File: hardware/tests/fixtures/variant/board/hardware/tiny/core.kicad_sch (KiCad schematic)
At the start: 2 parts

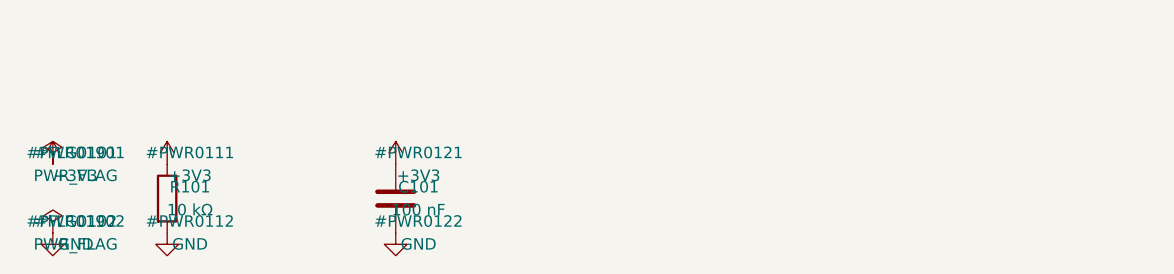
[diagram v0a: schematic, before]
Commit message: odapkit variant: absent-state check and software outputs per variant (RFC 0011 rules 2, 7, 8)
The absent-state check reads the XML netlist with the variant's resolution: every
net a dnp block touches is classified with the fitted parts only (single-pin,
floating, rail without source, defined) and matched to a declared absent state
from the block sheets' interface tables or the record's absent_state list; nets
touched only by other unfitted parts are reported when they become single-pin.
Findings absent.floating, absent.single-pin, absent.rail-unsourced,
absent.undeclared, absent.declared-mismatch and absent.not-applicable.

apply writes absent-state.json (opendap.variant-absent-state/v1),
software/capabilities.json (opendap.variant-capabilities/v1, a fragment for the
device description; consumer side open) and software/devicetree.json
(opendap.variant-devicetree/v1) with variant.dtso, status okay or disabled per
block node, blocks with no node listed as skipped. check runs the absent-state
check per variant. Block records gain structured absent_state and software;
the Markdown catalog reads its Absent state and Software rows. The fixture's
sensor sheet carries an interface table.

Co-Authored-By: Claude Opus 5.5 <noreply@anthropic.com>
Claude-Session: https://claude.ai/code/session_01Ei262h3TpgY9vyfNLMi5Mn
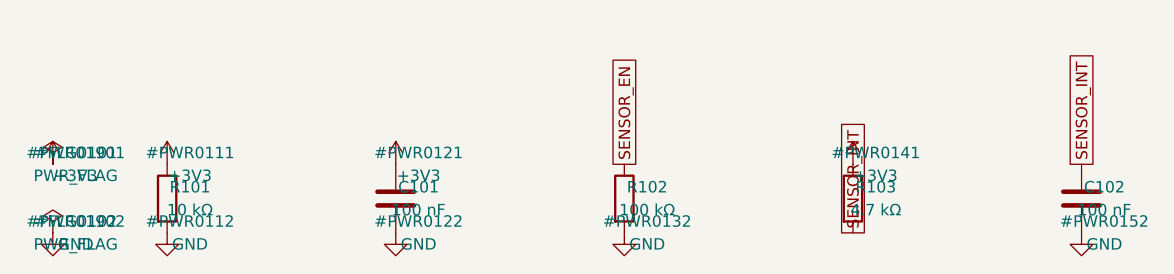
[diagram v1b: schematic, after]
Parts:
- added C102: 100 nF, Capacitor_SMD:C_0402_1005Metric, symbol Device:C
- added R102: 100 kΩ, Resistor_SMD:R_0603_1608Metric, symbol Device:R
- added R103: 4.7 kΩ, Resistor_SMD:R_0603_1608Metric, symbol Device:R
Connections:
- net +3V3: now also R103.1
- net GND: now also C102.2, R102.2
- new net SENSOR_EN: R102.1
- new net SENSOR_INT: C102.1, R103.2
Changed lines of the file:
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@@
   (instances (project "tiny" (path "/66a81b00-37dd-53f5-81ba-daabee42749a/791f5bf8-41bc-56d1-9e1d-b6f01e930073" (reference "#PWR0122") (unit 1))))
+)
+(symbol (lib_id "Device:R") (at 114.3 60.96 0) (unit 1) (body_style 1) (exclude_from_sim no) (in_bom yes) (on_board yes) (dnp no)
+  (property "Reference" "R102" (at 116.84 59.69 0) (effects (font (size 1.27 1.27))))
+  (property "Value" "100 kΩ" (at 116.84 62.230000000000004 0) (effects (font (size 1.27 1.27))))
+  (property "Footprint" "Resistor_SMD:R_0603_1608Metric" (at 114.3 60.96 0) (effects (font (size 1.27 1.27)) (hide yes)))
+  (property "Datasheet" "" (at 114.3 60.96 0) (effects (font (size 1.27 1.27)) (hide yes)))
+  (property "Block" "blk.core" (at 114.3 60.96 0) (effects (font (size 1.27 1.27)) (hide yes)))
+  (property "MPN" "RC0603FR-07100KL" (at 114.3 60.96 0) (effects (font (size 1.27 1.27)) (hide yes)))
+  (property "Manufacturer" "YAGEO" (at 114.3 60.96 0) (effects (font (size 1.27 1.27)) (hide yes)))
+  (pin "1")
+  (pin "2")
+  (instances (project "tiny" (path "/66a81b00-37dd-53f5-81ba-daabee42749a/791f5bf8-41bc-56d1-9e1d-b6f01e930073" (reference "R102") (unit 1))))
+)
+(global_label "SENSOR_EN" (shape passive) (at 114.3 57.15 90) (effects (font (size 1.27 1.27)) (justify left)))
+(symbol (lib_id "power:GND") (at 114.3 64.77 0) (unit 1) (body_style 1) (exclude_from_sim no) (in_bom no) (on_board no) (dnp no)
+  (property "Reference" "#PWR0132" (at 116.84 63.49999999999999 0) (effects (font (size 1.27 1.27))))
+  (property "Value" "GND" (at 116.84 66.03999999999999 0) (effects (font (size 1.27 1.27))))
+  (property "Footprint" "" (at 114.3 64.77 0) (effects (font (size 1.27 1.27)) (hide yes)))
+  (property "Datasheet" "" (at 114.3 64.77 0) (effects (font (size 1.27 1.27)) (hide yes)))
+  (pin "1")
+  (instances (project "tiny" (path "/66a81b00-37dd-53f5-81ba-daabee42749a/791f5bf8-41bc-56d1-9e1d-b6f01e930073" (reference "#PWR0132") (unit 1))))
+)
+(symbol (lib_id "Device:R") (at 139.7 60.96 0) (unit 1) (body_style 1) (exclude_from_sim no) (in_bom yes) (on_board yes) (dnp no)
+  (property "Reference" "R103" (at 142.23999999999998 59.69 0) (effects (font (size 1.27 1.27))))
+  (property "Value" "4.7 kΩ" (at 142.23999999999998 62.230000000000004 0) (effects (font (size 1.27 1.27))))
+  (property "Footprint" "Resistor_SMD:R_0603_1608Metric" (at 139.7 60.96 0) (effects (font (size 1.27 1.27)) (hide yes)))
+  (property "Datasheet" "" (at 139.7 60.96 0) (effects (font (size 1.27 1.27)) (hide yes)))
+  (property "Block" "blk.core" (at 139.7 60.96 0) (effects (font (size 1.27 1.27)) (hide yes)))
+  (property "MPN" "RC0603FR-074K7L" (at 139.7 60.96 0) (effects (font (size 1.27 1.27)) (hide yes)))
+  (property "Manufacturer" "YAGEO" (at 139.7 60.96 0) (effects (font (size 1.27 1.27)) (hide yes)))
+  (pin "1")
+  (pin "2")
+  (instances (project "tiny" (path "/66a81b00-37dd-53f5-81ba-daabee42749a/791f5bf8-41bc-56d1-9e1d-b6f01e930073" (reference "R103") (unit 1))))
+)
+(symbol (lib_id "power:+3V3") (at 139.7 57.15 0) (unit 1) (body_style 1) (exclude_from_sim no) (in_bom no) (on_board no) (dnp no)
+  (property "Reference" "#PWR0141" (at 142.23999999999998 55.879999999999995 0) (effects (font (size 1.27 1.27))))
+  (property "Value" "+3V3" (at 142.23999999999998 58.42 0) (effects (font (size 1.27 1.27))))
+  (property "Footprint" "" (at 139.7 57.15 0) (effects (font (size 1.27 1.27)) (hide yes)))
+  (property "Datasheet" "" (at 139.7 57.15 0) (effects (font (size 1.27 1.27)) (hide yes)))
+  (pin "1")
+  (instances (project "tiny" (path "/66a81b00-37dd-53f5-81ba-daabee42749a/791f5bf8-41bc-56d1-9e1d-b6f01e930073" (reference "#PWR0141") (unit 1))))
+)
+(global_label "SENSOR_INT" (shape passive) (at 139.7 64.77 90) (effects (font (size 1.27 1.27)) (justify left)))
+(symbol (lib_id "Device:C") (at 165.1 60.96 0) (unit 1) (body_style 1) (exclude_from_sim no) (in_bom yes) (on_board yes) (dnp no)
+  (property "Reference" "C102" (at 167.64 59.69 0) (effects (font (size 1.27 1.27))))
+  (property "Value" "100 nF" (at 167.64 62.230000000000004 0) (effects (font (size 1.27 1.27))))
+  (property "Footprint" "Capacitor_SMD:C_0402_1005Metric" (at 165.1 60.96 0) (effects (font (size 1.27 1.27)) (hide yes)))
+  (property "Datasheet" "" (at 165.1 60.96 0) (effects (font (size 1.27 1.27)) (hide yes)))
+  (property "Block" "blk.core" (at 165.1 60.96 0) (effects (font (size 1.27 1.27)) (hide yes)))
+  (property "MPN" "GRM155R71C104KA88D" (at 165.1 60.96 0) (effects (font (size 1.27 1.27)) (hide yes)))
+  (property "Manufacturer" "Murata" (at 165.1 60.96 0) (effects (font (size 1.27 1.27)) (hide yes)))
+  (pin "1")
+  (pin "2")
+  (instances (project "tiny" (path "/66a81b00-37dd-53f5-81ba-daabee42749a/791f5bf8-41bc-56d1-9e1d-b6f01e930073" (reference "C102") (unit 1))))
+)
+(global_label "SENSOR_INT" (shape passive) (at 165.1 57.15 90) (effects (font (size 1.27 1.27)) (justify left)))
+(symbol (lib_id "power:GND") (at 165.1 64.77 0) (unit 1) (body_style 1) (exclude_from_sim no) (in_bom no) (on_board no) (dnp no)
+  (property "Reference" "#PWR0152" (at 167.64 63.49999999999999 0) (effects (font (size 1.27 1.27))))
+  (property "Value" "GND" (at 167.64 66.03999999999999 0) (effects (font (size 1.27 1.27))))
+  (property "Footprint" "" (at 165.1 64.77 0) (effects (font (size 1.27 1.27)) (hide yes)))
+  (property "Datasheet" "" (at 165.1 64.77 0) (effects (font (size 1.27 1.27)) (hide yes)))
+  (pin "1")
+  (instances (project "tiny" (path "/66a81b00-37dd-53f5-81ba-daabee42749a/791f5bf8-41bc-56d1-9e1d-b6f01e930073" (reference "#PWR0152") (unit 1))))
 )
 (symbol (lib_id "power:PWR_FLAG") (at 50.8 57.15 0) (unit 1) (body_style 1) (exclude_from_sim no) (in_bom no) (on_board no) (dnp no)
